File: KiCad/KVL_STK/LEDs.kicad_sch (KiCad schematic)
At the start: 60 parts

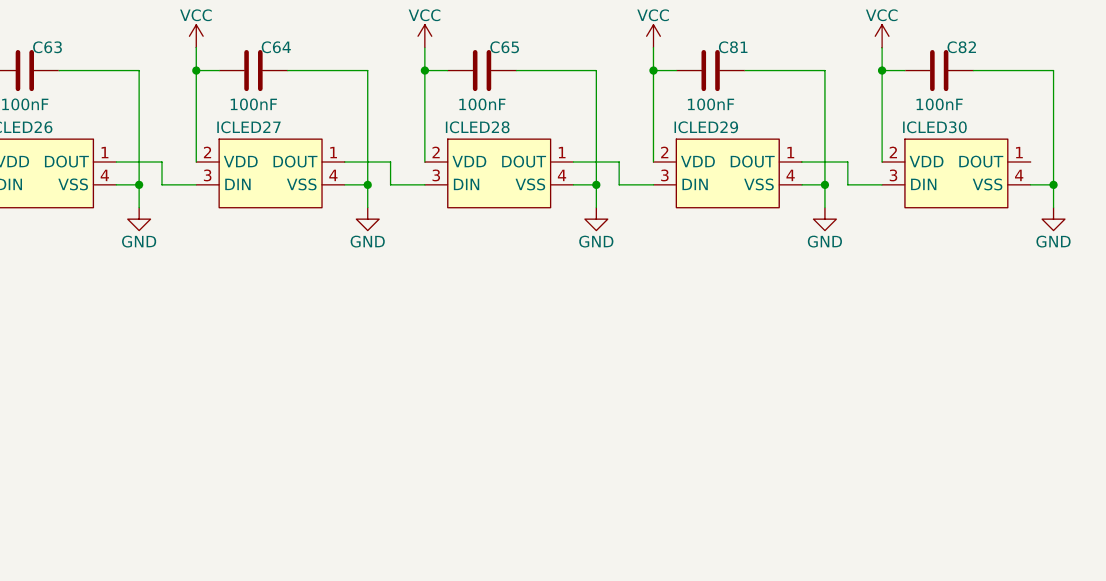
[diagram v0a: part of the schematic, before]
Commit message: Added four LEDs.
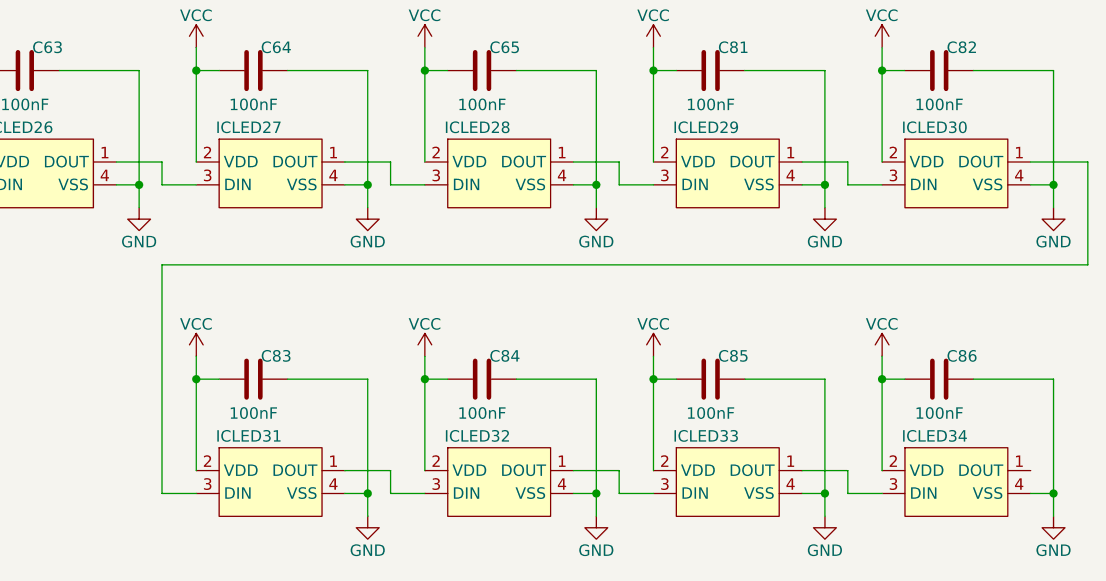
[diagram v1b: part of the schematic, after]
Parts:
- added C83, C84, C85, C86: 100nF, Capacitor_SMD:C_0402_1005Metric, symbol Device:C
- added ICLED31, ICLED32, ICLED33, ICLED34: ~, My_Parts:1312020030000, symbol My_Parts:Address_LED
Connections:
- net GND: now also C83.2, C84.2, C85.2, C86.2, ICLED31.4 (VSS), ICLED32.4 (VSS), ICLED33.4 (VSS), ICLED34.4 (VSS)
- net VCC: now also C83.1, C84.1, C85.1, C86.1, ICLED31.2 (VDD), ICLED32.2 (VDD), ICLED33.2 (VDD), ICLED34.2 (VDD)
- net at ICLED30.1 (DOUT): now also ICLED31.3 (DIN)
- new net: ICLED33.1 (DOUT), ICLED34.3 (DIN)
- new net: ICLED32.1 (DOUT), ICLED33.3 (DIN)
- new net: ICLED31.1 (DOUT), ICLED32.3 (DIN)
